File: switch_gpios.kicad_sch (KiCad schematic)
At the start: 40 parts

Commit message: uses SPI2 instead of SPI in name. Refs: #1
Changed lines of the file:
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@@
 	(bus
 		(pts
-			(xy 49.53 129.54) (xy 55.88 129.54)
+			(xy 53.34 129.54) (xy 55.88 129.54)
 		)
 		(stroke
@@
 		)
 	)
-	(hierarchical_label "SPI_STM_SWITCH{MOSI,MISO,nCS,CLK}"
+	(hierarchical_label "SPI2_STM_SWITCH{MOSI,MISO,nCS,CLK}"
 		(shape bidirectional)
-		(at 49.53 129.54 180)
-		(effects
-			(font
+		(at 53.34 129.54 180)
+		(effects
+			(font

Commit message: fixes incorrect SPI2 naming on switch sheets. Refs: #1
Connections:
- net SPI_STM_SWITCH.CLK renamed SPI2_STM_SWITCH.CLK
- net SPI_STM_SWITCH.MISO renamed SPI2_STM_SWITCH.MISO
- net SPI_STM_SWITCH.MOSI renamed SPI2_STM_SWITCH.MOSI
- net SPI_STM_SWITCH.nCS renamed SPI2_STM_SWITCH.nCS
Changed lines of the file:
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@@
 		)
 	)
-	(label "SPI_STM_SWITCH.MOSI"
+	(label "SPI2_STM_SWITCH.MOSI"
 		(at 59.69 154.94 0)
 		(effects
@@
 		)
 	)
-	(label "SPI_STM_SWITCH.MISO"
+	(label "SPI2_STM_SWITCH.MISO"
 		(at 59.69 147.32 0)
 		(effects
@@
 		)
 	)
-	(label "SPI_STM_SWITCH.nCS"
+	(label "SPI2_STM_SWITCH.nCS"
 		(at 59.69 139.7 0)
 		(effects
@@
 		)
 	)
-	(label "SPI_STM_SWITCH.CLK"
+	(label "SPI2_STM_SWITCH.CLK"
 		(at 59.69 132.08 0)
 		(effects

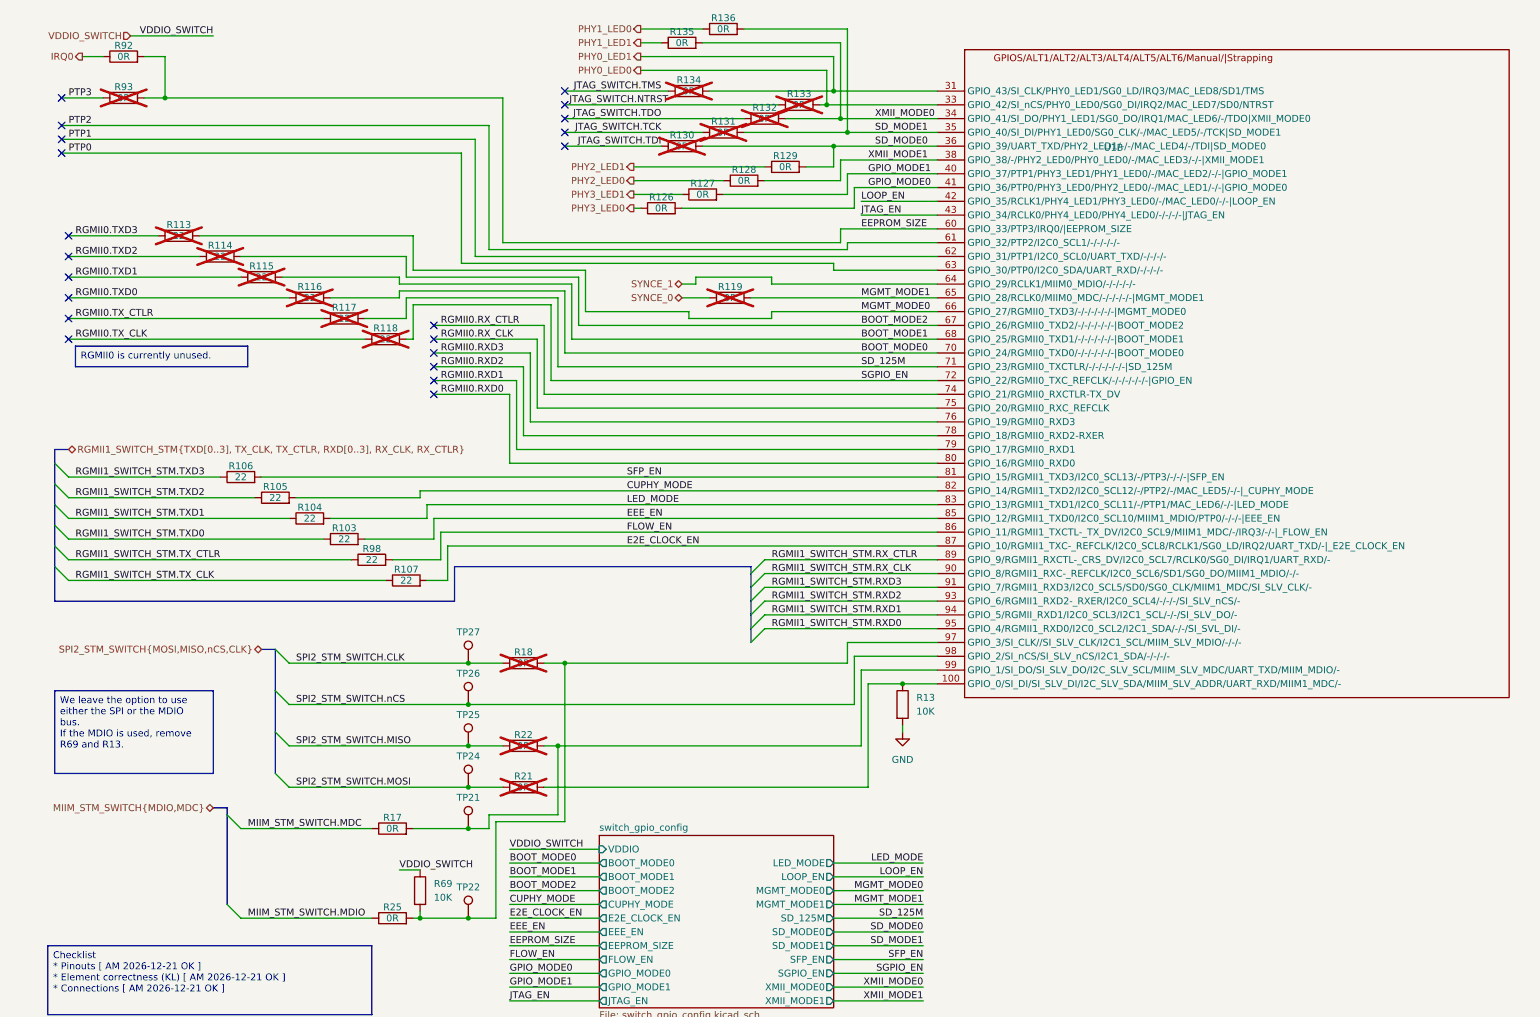
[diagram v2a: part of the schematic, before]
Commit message: RGMII1 bus uses Microchip names. Refs: #1
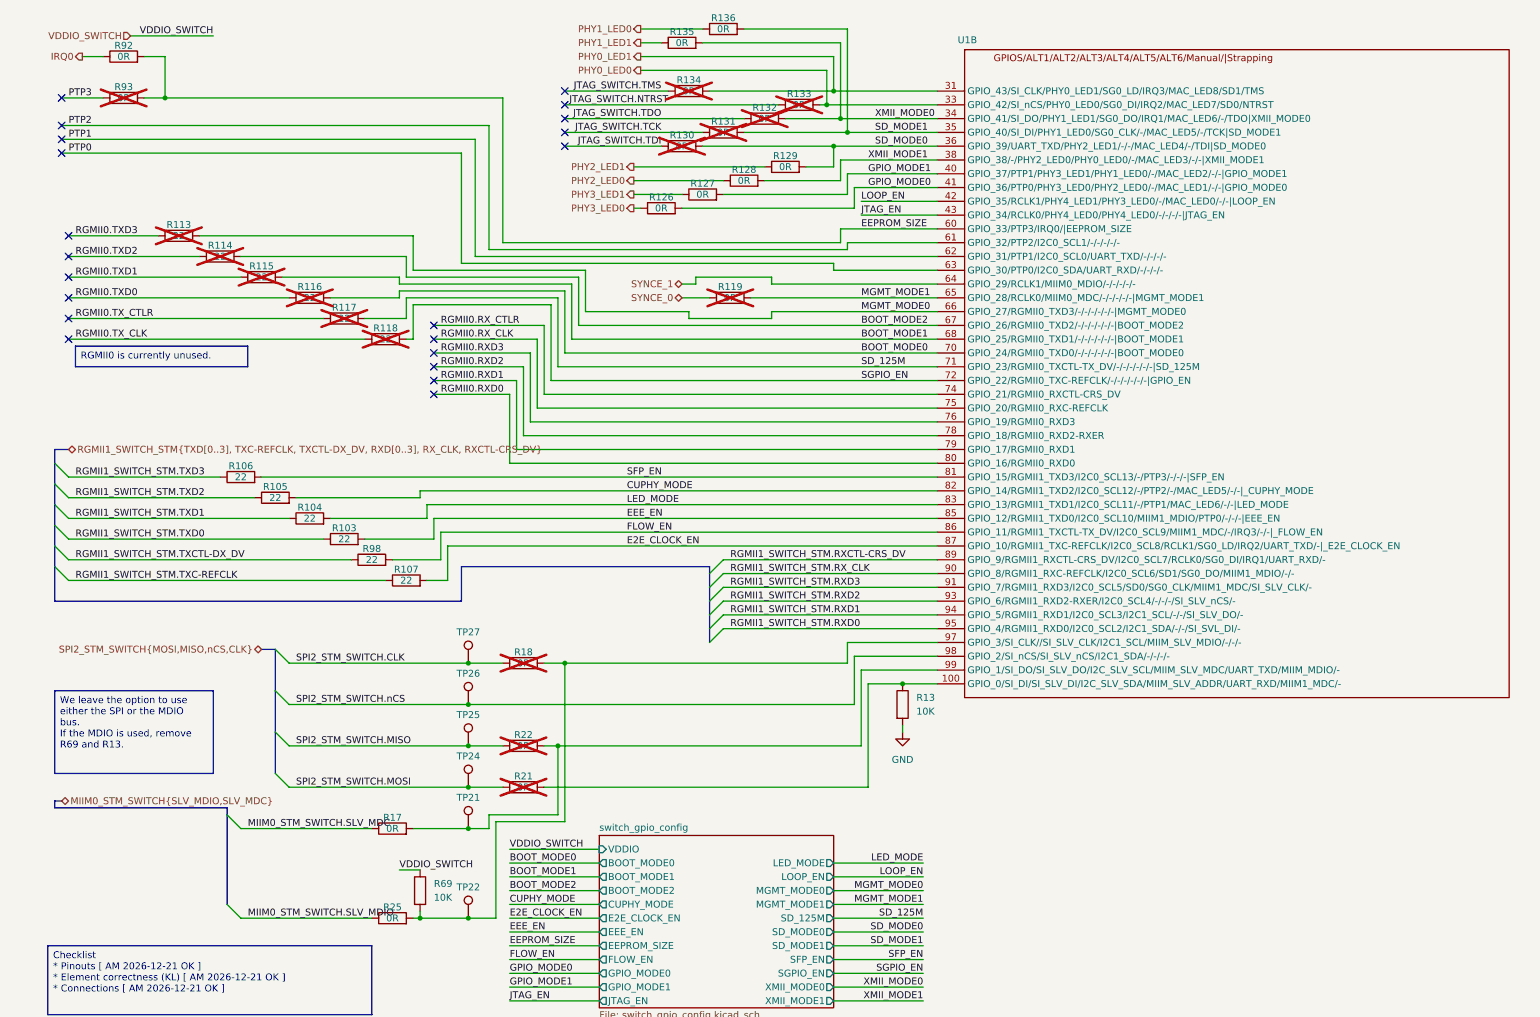
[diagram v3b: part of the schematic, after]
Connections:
- net MIIM_STM_SWITCH.MDC renamed MIIM0_STM_SWITCH.SLV_MDC
- net MIIM_STM_SWITCH.MDIO renamed MIIM0_STM_SWITCH.SLV_MDIO
- net RGMII1_SWITCH_STM.RX_CTLR renamed RGMII1_SWITCH_STM.RXCTL-CRS_DV
- net RGMII1_SWITCH_STM.TX_CLK renamed RGMII1_SWITCH_STM.TXC-REFCLK
- net RGMII1_SWITCH_STM.TX_CTLR renamed RGMII1_SWITCH_STM.TXCTL-DX_DV

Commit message: updates component details for ordering. Refs: #1
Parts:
- TP21, TP22, TP24, TP25, TP26, TP27: now left out of the parts list
- U1: value ~ -> LAN96455F-I/8MW; Digikey (none) -> 150-LAN96455F-I/8MW-ND; Mouser (none) -> 579-LAN96455FI8MW; manf# LAN96455F-I/8MW -> (none)

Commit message: 20: swapping RGMII port from RGMII1 to RGMII0
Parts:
- R103, R104, R105, R106, R107, R98: now not fitted
- R113, R114, R115, R116, R117, R118: now fitted
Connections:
- net RGMII0.RXD0 renamed RGMII0_SWITCH_STM.RXD0
- net RGMII0.RXD1 renamed RGMII0_SWITCH_STM.RXD1
- net RGMII0.RXD2 renamed RGMII0_SWITCH_STM.RXD2
- net RGMII0.RXD3 renamed RGMII0_SWITCH_STM.RXD3
- net RGMII0.RX_CLK renamed RGMII0_SWITCH_STM.RX_CLK
- net RGMII0.RX_CTLR renamed RGMII0_SWITCH_STM.RXCTL-CRS_DV
- net RGMII0.TXD0 renamed RGMII0_SWITCH_STM.TXD0
- net RGMII0.TXD1 renamed RGMII0_SWITCH_STM.TXD1
- net RGMII0.TXD2 renamed RGMII0_SWITCH_STM.TXD2
- net RGMII0.TXD3 renamed RGMII0_SWITCH_STM.TXD3
- net RGMII0.TX_CLK renamed RGMII0_SWITCH_STM.TXC-REFCLK
- net RGMII0.TX_CTLR renamed RGMII0_SWITCH_STM.TXCTL-DX_DV
- no-connect marks 21 -> 9

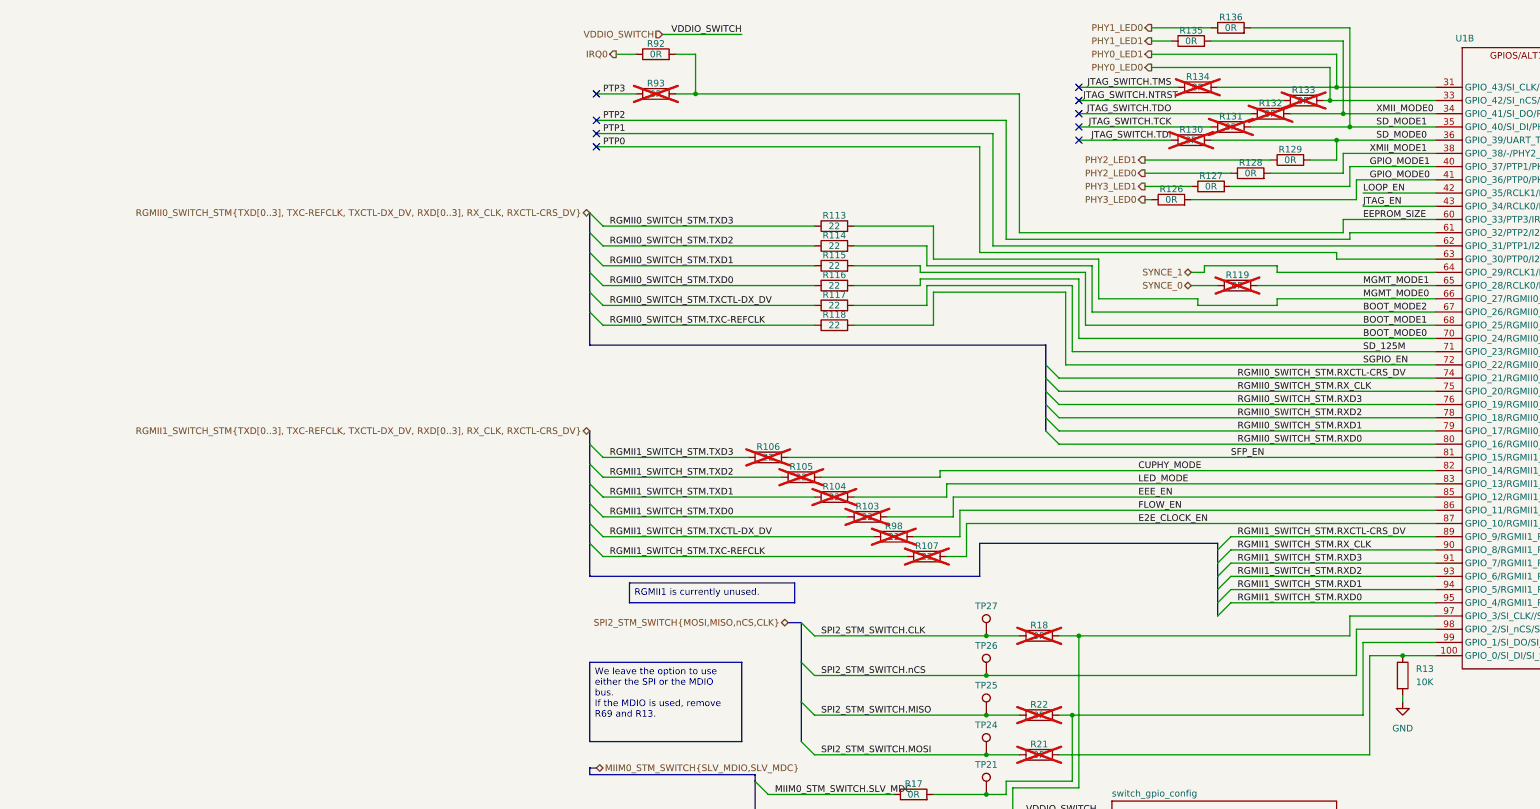
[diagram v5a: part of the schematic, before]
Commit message: clean up and fix on controller. Refs: #20
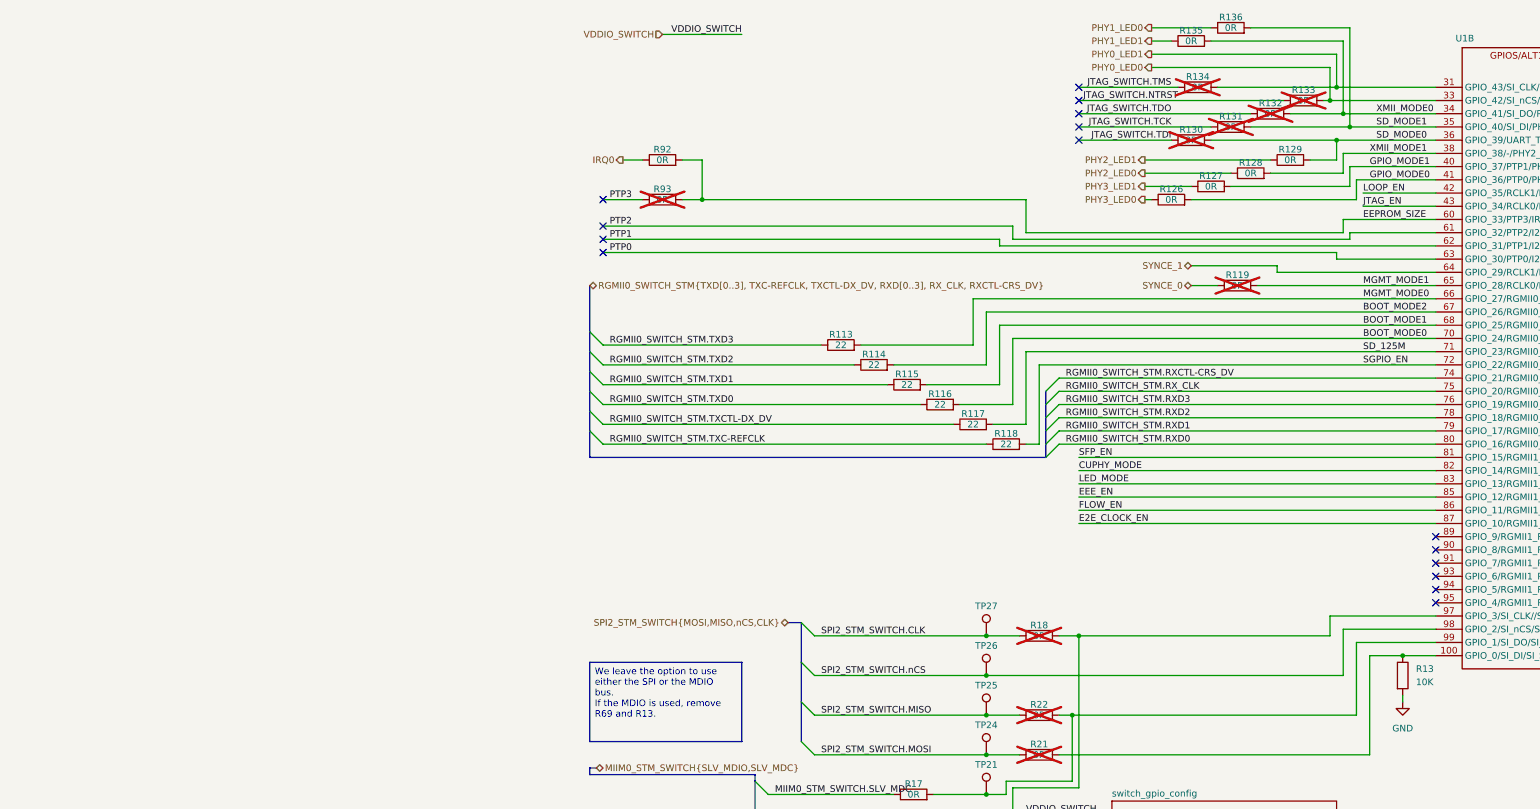
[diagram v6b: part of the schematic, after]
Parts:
- removed R103, R104, R105, R106, R107, R98: 22, KL_Footprints:R_0603, symbol KL_R:R_22_100mW_1pct_0603
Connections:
- net RGMII1_SWITCH_STM.RXCTL-CRS_DV: no longer names the net of U1.89 (GPIO_9/RGMII1_RXCTL-CRS_DV/I2C0_SCL7/RCLK0/SG0_DI/IRQ1/UART_RXD/-)
- net RGMII1_SWITCH_STM.RXD0: no longer names the net of U1.95 (GPIO_4/RGMII1_RXD0/I2C0_SCL2/I2C1_SDA/-/-/SI_SVL_DI/-)
- net RGMII1_SWITCH_STM.RXD1: no longer names the net of U1.94 (GPIO_5/RGMII1_RXD1/I2C0_SCL3/I2C1_SCL/-/-/SI_SLV_DO/-)
- net RGMII1_SWITCH_STM.RXD2: no longer names the net of U1.93 (GPIO_6/RGMII1_RXD2-RXER/I2C0_SCL4/-/-/-/SI_SLV_nCS/-)
- net RGMII1_SWITCH_STM.RXD3: no longer names the net of U1.91 (GPIO_7/RGMII1_RXD3/I2C0_SCL5/SD0/SG0_CLK/MIIM1_MDC/SI_SLV_CLK/-)
- net RGMII1_SWITCH_STM.RX_CLK: no longer names the net of U1.90 (GPIO_8/RGMII1_RXC-REFCLK/I2C0_SCL6/SD1/SG0_DO/MIIM1_MDIO/-/-)
- no-connect marks 9 -> 15
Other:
- moved on the sheet: R113, R114, R115, R116, R117, R118, R92, R93
